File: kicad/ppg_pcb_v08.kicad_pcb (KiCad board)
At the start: 4 copper layers, 13.5 x 13.5 mm, 26 parts, among them J1 12V, J2 GND, J3 TXP, J4 TXN, J5 RXP, J6 RXN, J7 SWDIO, J8 SWCLK, J9 NRST, U1 MAXM86161EFD+, U2 STM32C011F6U6, U3 SN65LVDS1DBVR, U4 MCP1703A-5002E/MC, U5 MCP1703A-3302E/MC, U6 SN65LVDT2DBVR

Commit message: Import RS-422 project snapshot from MVP-PPG.zip
Preserve all 375 archive files, including KiCad sources, BOM, documentation, datasheets and historical snapshots.

Validation: ZIP CRC verified; committed paths and file hashes match the archive.
Source archive SHA-256: 3fbf3dc2505b0eca75517d05229e315a4e9136078cfb812aac535ee66e8536a6
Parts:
- added D1: SPHV15-01ETG, SleepBud:TVS_SOD882_1x0.6, B.Cu at (17.8, 11.5)
- added D6: ESD351DPYR, SleepBud:TI_DPY0002A_1x0.6, B.Cu at (20.9, 19.5)
- added D7: ESD351DPYR, SleepBud:TI_DPY0002A_1x0.6, B.Cu at (23.5, 15.9)
- added D8: ESD351DPYR, SleepBud:TI_DPY0002A_1x0.6, B.Cu at (16.5, 17.4)
- added FB1: BLM15PX601SN1D, Inductor_SMD:L_0402_1005Metric, B.Cu at (20.9, 11.1)
- added R3: 120/1%, Resistor_SMD:R_0402_1005Metric, B.Cu at (14.1, 17.9)
- added R4: 10k, Resistor_SMD:R_0201_0603Metric, B.Cu at (25.8, 16.0)
- added R5: 22, Resistor_SMD:R_0402_1005Metric, B.Cu at (23.1, 17.8)
- added R6: 22, Resistor_SMD:R_0402_1005Metric, B.Cu at (24.7, 16.9)
- added R7: 22, Resistor_SMD:R_0402_1005Metric, B.Cu at (15.3, 17.7)
- added R8: 22, Resistor_SMD:R_0402_1005Metric, B.Cu at (15.1, 16.2)
- C1, C13: footprint C_0402_1005Metric -> Capacitor_SMD:C_0402_1005Metric
- C11, C12, C14, C4, C5, C6, C7: footprint C_0201_0603Metric -> Capacitor_SMD:C_0201_0603Metric
- R1, R2: footprint R_0201_0603Metric -> Resistor_SMD:R_0201_0603Metric
- U2: footprint ST_UFQFPN-20_3x3mm_P0.5mm -> Package_DFN_QFN:ST_UFQFPN-20_3x3mm_P0.5mm
- U3: value SN65LVDS1DBVR -> XR33194; footprint SOT-23-5 -> SleepBud:TSOT23-6_MaxLinear
- U4, U5: footprint DFN-8-1EP_2x3mm_P0.5mm_EP0.61x2.2mm -> Package_DFN_QFN:DFN-8-1EP_2x3mm_P0.5mm_EP0.61x2.2mm
- U6: value SN65LVDT2DBVR -> XR33183; footprint SOT-23-5 -> SleepBud:TSOT23-6_MaxLinear
- moved C11 33.6 mm to (20.3, 20.6), turned to -90 degrees
- moved J7 30.1 mm to (23.7, 18.8), turned to 0 degrees
- moved J9 30.0 mm to (16.7, 18.4), turned to -45 degrees
- moved U2 29.3 mm to (20.1, 17.3), turned to 90 degrees
- moved J6 29.1 mm to (14.8, 19.6), turned to 90 degrees
- moved C13 27.8 mm to (16.2, 21.2), turned to -90 degrees
- moved C7 27.8 mm to (20.5, 12.3), turned to 45 degrees
- moved J4 27.6 mm to (25.1, 18.7)
- moved C6 27.2 mm to (25.3, 14.2), turned to -45 degrees
- moved J8 27.0 mm to (22.8, 16.6), turned to 135 degrees
- moved U5 26.8 mm to (22.8, 21.1), turned to 45 degrees
- moved J2 26.7 mm to (20.7, 22.7), turned to -135 degrees
- moved U4 26.5 mm to (18.3, 21.5), turned to 180 degrees
- moved U1 26.2 mm to (20.0, 17.0)
- moved C14 26.1 mm to (24.7, 20.2), turned to -45 degrees
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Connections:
- net NRST renamed /NRST
- net SCL renamed /SCL
- net SDA renamed /SDA
- net SWCLK renamed /SWCLK
- net SWDIO renamed /SWDIO
- net VLDO renamed /VLDO
- net VREF renamed /VREF
- J1 pad 1: 12V -> /12V_IN
- J3 pad 1: TXP -> /TXP
- J4 pad 1: TXN -> /TXN
- J5 pad 1: RXP -> /RXP
- J6 pad 1: RXN -> /RXN
- U1 pad 13: (no net) -> unconnected-(U1-GPIO-Pad13)
- U1 pad 14: (no net) -> unconnected-(U1-INTB-Pad14)
- U1 pad 6: (no net) -> unconnected-(U1-NC-Pad6)
- U1 pad 7: (no net) -> unconnected-(U1-NC-Pad7)
- U1 pad 8: (no net) -> unconnected-(U1-NC-Pad8)
- U2 pad 1: (no net) -> unconnected-(U2-PC15-Pad1)
- U2 pad 10: (no net) -> unconnected-(U2-PA5-Pad10)
- U2 pad 11: (no net) -> unconnected-(U2-PA6-Pad11)
- U2 pad 12: (no net) -> unconnected-(U2-PA7-Pad12)
- U2 pad 13: (no net) -> unconnected-(U2-PA8-Pad13)
- U2 pad 14: UART_TX -> /UART_TX
- U2 pad 15: UART_RX -> /UART_RX
- U2 pad 20: (no net) -> unconnected-(U2-PC14-Pad20)
- U2 pad 5: (no net) -> unconnected-(U2-PA0-Pad5)
- U2 pad 6: (no net) -> unconnected-(U2-PA1-Pad6)
- U2 pad 7: (no net) -> unconnected-(U2-PA2-Pad7)
- U2 pad 8: (no net) -> unconnected-(U2-PA3-Pad8)
- U2 pad 9: (no net) -> unconnected-(U2-PA4-Pad9)
- U3 pad 1: 3V3 -> /UART_TX
- U3 pad 2: GND -> 3V3
- U3 pad 3: TXN -> 3V3
- U3 pad 4: TXP -> /TXN_DRV
- U3 pad 5: UART_TX -> GND
- U4 pad 2: (no net) -> unconnected-(U4-NC-Pad2)
- U4 pad 3: (no net) -> unconnected-(U4-NC-Pad3)
- U4 pad 5: (no net) -> unconnected-(U4-NC-Pad5)
- U4 pad 6: (no net) -> unconnected-(U4-NC-Pad6)
- U4 pad 7: (no net) -> unconnected-(U4-NC-Pad7)
- U5 pad 2: (no net) -> unconnected-(U5-NC-Pad2)
- U5 pad 3: (no net) -> unconnected-(U5-NC-Pad3)
- U5 pad 5: (no net) -> unconnected-(U5-NC-Pad5)
- U5 pad 6: (no net) -> unconnected-(U5-NC-Pad6)
- U5 pad 7: (no net) -> unconnected-(U5-NC-Pad7)
- U6 pad 3: RXP -> /UART_RX
- U6 pad 4: RXN -> /RXN_RCV
- U6 pad 5: UART_RX -> GND
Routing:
- net 3V3: track 17.3 -> 35.1 mm, vias 5 -> 10
- net GND: track 33.9 -> 17.5 mm, vias 5 -> 18
- net /UART_TX: track 0.00 -> 12.3 mm, vias 0 -> 2
- net 12V: track 4.83 -> 14.2 mm, vias 0 -> 2
- net /UART_RX: track 0.00 -> 9.07 mm, vias 0 -> 2
- net /TXP_DRV: track 0.00 -> 8.72 mm, vias 0 -> 2
- net UART_RX: track 7.70 -> 0.00 mm, vias 2 -> 0
- net UART_TX: track 7.47 -> 0.00 mm, vias 2 -> 0
- net /RXP: track 0.00 -> 6.70 mm, vias 0 -> 2
- net /TXN_DRV: track 0.00 -> 6.62 mm, vias 0 -> 2
- net /SWDIO: track 2.34 -> 7.72 mm, vias 0 -> 3
- net /RXP_RCV: track 0.00 -> 5.38 mm, vias 0 -> 2
- net /SCL: track 3.96 -> 8.68 mm, vias 1 -> 2
- net /VREF: track 3.13 -> 7.34 mm
- net /TXP: track 0.00 -> 4.03 mm, vias 0 -> 2
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- added copper zone on F.Cu, net GND
- removed copper zone on In2.Cu, net 3V3

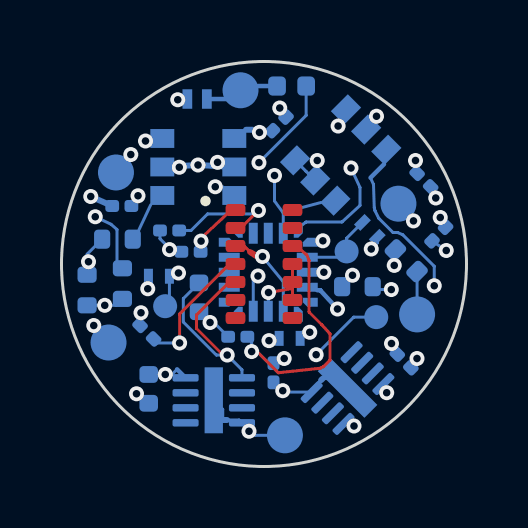
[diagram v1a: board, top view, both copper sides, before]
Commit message: Save PPG routing, UART adapter, BOMs and 10-set panel
Record the current PPG schematic and routed six-layer PCB, UART adapter
with mounting holes, and default 0.25 mm via drill policy.

Include UART quantity BOMs in the requested PPG format and the validated
10-set PPG/UART panel Gerbers, drill files, placement coordinates and
review history. Preserve earlier manufacturing inputs and exclude local
backups, editor state and spreadsheet inspection caches.

Validation: current PPG/UART PCB hashes match the panel manifest; panel
ZIP CRC and checksums pass; 29 Python source files parse successfully.
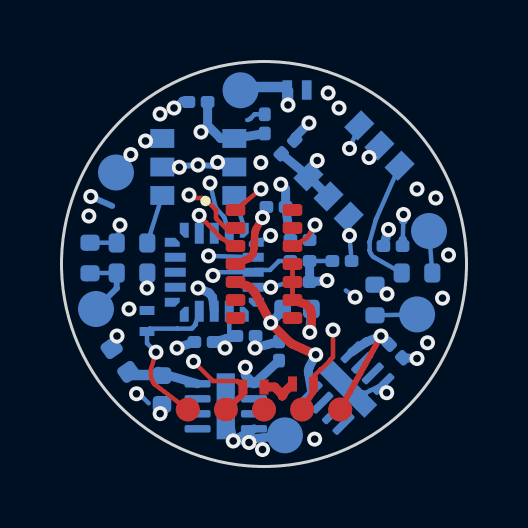
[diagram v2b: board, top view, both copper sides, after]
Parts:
- added C15: 100 nF, Capacitor_SMD:C_0201_0603Metric, B.Cu at (19.4, 19.4)
- added C16: 100 nF, Capacitor_SMD:C_0201_0603Metric, B.Cu at (24.3, 16.4)
- added C17: 100 nF, Capacitor_SMD:C_0201_0603Metric, B.Cu at (20.5, 19.9)
- added J10: GND, SleepBud:TestPad_D0.8_Front, F.Cu at (20.0, 21.9)
- added J11: 3V3_VTREF, SleepBud:TestPad_D0.8_Front, F.Cu at (22.5, 21.9)
- C1: value 10uF 6.3V X5R -> 10 µF
- C11, C6, C7: value 100nF -> 100 nF
- C12, C14, C4, C5: value 1uF 6.3V -> 1 µF
- C13: value 1uF 25V X7R -> 1 µF
- D6, D7: moved to F.Cu
- J7, J8, J9: footprint SleepBud:CablePad_D0.8 -> SleepBud:TestPad_D0.8_Front; moved to F.Cu
- R1, R2: value 4.7k -> 4.7 kΩ
- R3: value 120/1% -> 120 Ω
- R4: value 10k -> 10 kΩ
- R5, R6, R7, R8: value 22 -> 22 Ω
- U3: value XR33194 -> XR33194ESBTR
- U6: value XR33183 -> XR33183ESBTR
- moved FB1 10.8 mm to (15.2, 20.2), turned to -55 degrees
- moved C4 6.00 mm to (20.4, 15.1), turned to 0 degrees
- moved J7 5.88 mm to (18.7, 21.9)
- moved J6 5.67 mm to (15.1, 13.9)
- moved D7 5.60 mm to (21.3, 21.0), turned to 180 degrees
- moved J8 5.47 mm to (21.3, 21.9), turned to 0 degrees
- moved C6 4.66 mm to (20.8, 13.1), turned to 45 degrees
- moved J5 4.60 mm to (14.4, 18.5)
- moved R2 4.46 mm to (21.2, 16.9), turned to 0 degrees
- moved C12 4.30 mm to (17.8, 11.6)
- moved C5 3.84 mm to (21.2, 16.2)
- moved R1 3.77 mm to (21.2, 17.6), turned to 0 degrees
- moved J9 3.53 mm to (17.5, 21.9), turned to 0 degrees
- moved R4 3.35 mm to (22.6, 16.9), turned to 180 degrees
- moved D1 3.34 mm to (21.1, 11.2), turned to 0 degrees
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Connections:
- U1 pad 3: 3V3 -> /LDO_EN
- U2 pad 12: unconnected-(U2-PA7-Pad12) -> /LDO_EN
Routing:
- net /12V_IN: track 2.52 -> 14.4 mm, vias 0 -> 3
- net 12V: track 14.2 -> 2.38 mm, vias 2 -> 0
- net /UART_RX: track 9.07 -> 1.13 mm, vias 2 -> 0
- net /SWCLK: track 2.58 -> 9.05 mm, vias 0 -> 2
- net /VREF: track 7.34 -> 1.59 mm
- net GND: track 17.5 -> 22.6 mm, vias 18 -> 32
- net /SDA: track 10.8 -> 6.39 mm
- net /TXP_DRV: track 8.72 -> 4.36 mm, vias 2 -> 0
- net /RXP: track 6.70 -> 2.56 mm, vias 2 -> 0
- net /UART_TX: track 12.3 -> 8.69 mm
- net /TXP: track 4.03 -> 1.40 mm, vias 2 -> 0
- net 5V_LED: track 14.5 -> 11.9 mm, vias 2 -> 3
- net /LDO_EN: track 0.00 -> 2.19 mm, vias 0 -> 1
- net /VLDO: track 4.44 -> 2.34 mm
- net /SWDIO: track 7.72 -> 9.66 mm, vias 3 -> 2
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- added copper zone on B.Cu, net GND
- added copper zone on In2.Cu, net GND
- added copper zone on In3.Cu, net GND
- added copper zone on In4.Cu, net GND
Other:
- copper layers 4 -> 6
